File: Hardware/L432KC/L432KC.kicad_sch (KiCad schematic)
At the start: 41 parts, among them J1 L4_G4, J2 USB_B_Micro, J3 JTAG, J4 3v3, J5 GND, J6 Conn_01x09, J7 Conn_01x08, J8 TVCC, J9 LogicAna, U1 AD8531ARTZ, U2 SRV05-4, U3 NUCLEO-L432KC, U4 TXB0304RUT, U5 TXB0304RUT

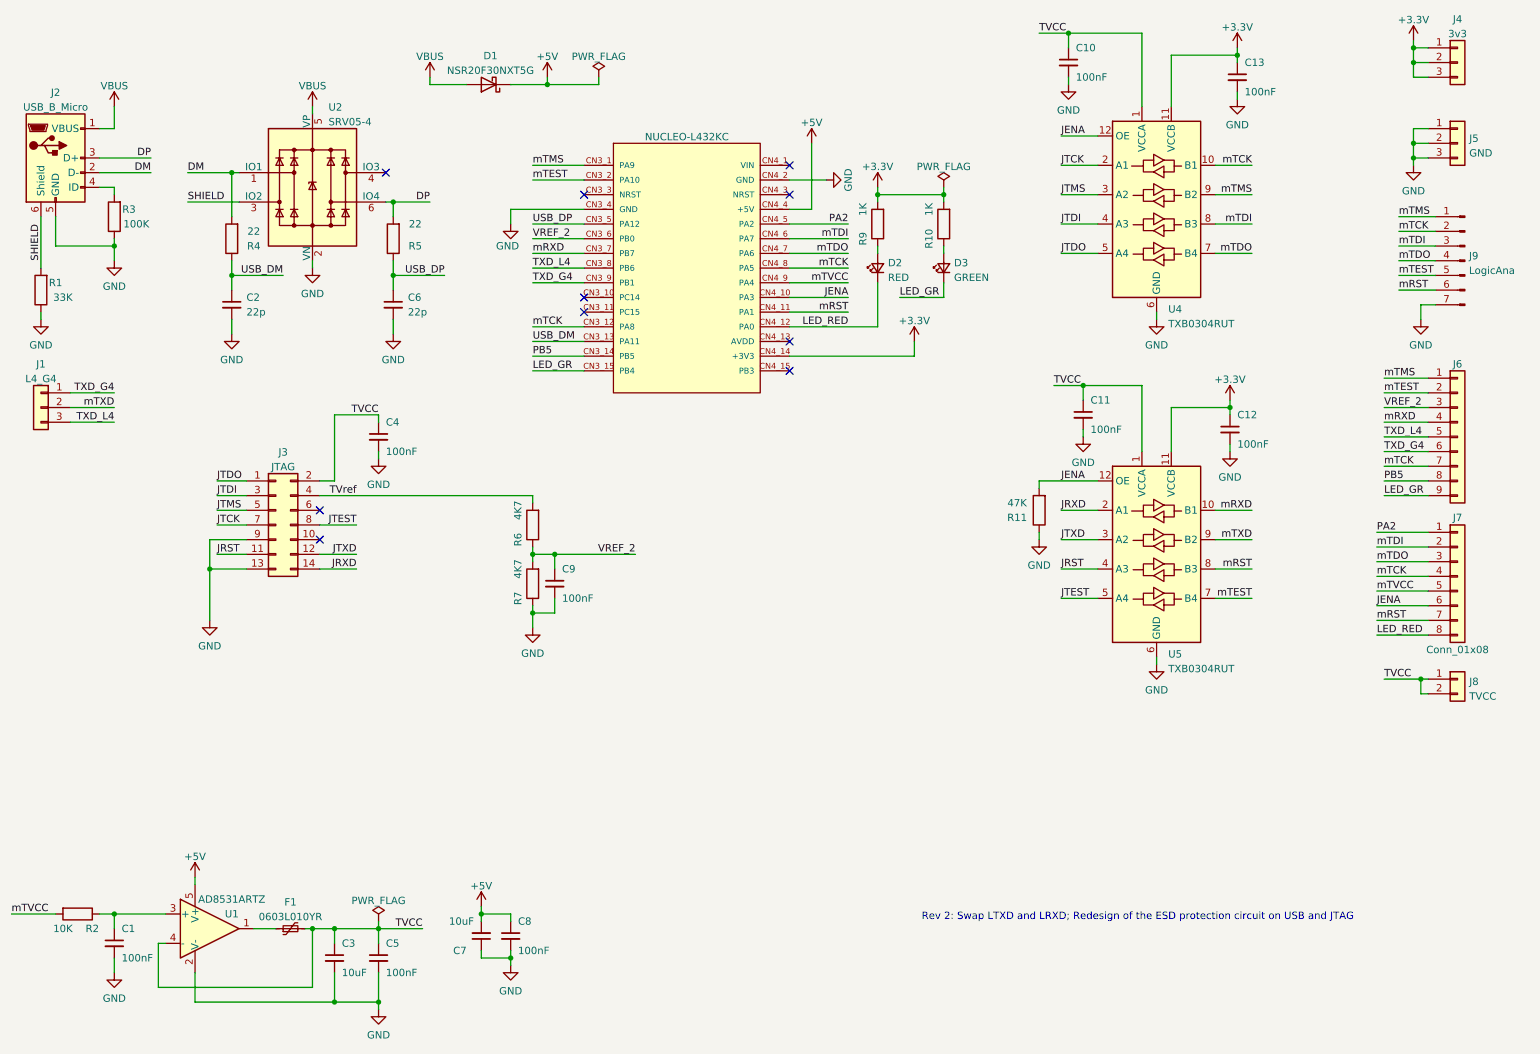
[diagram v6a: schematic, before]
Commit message: Updated L432KC/G431K6 prototype board.
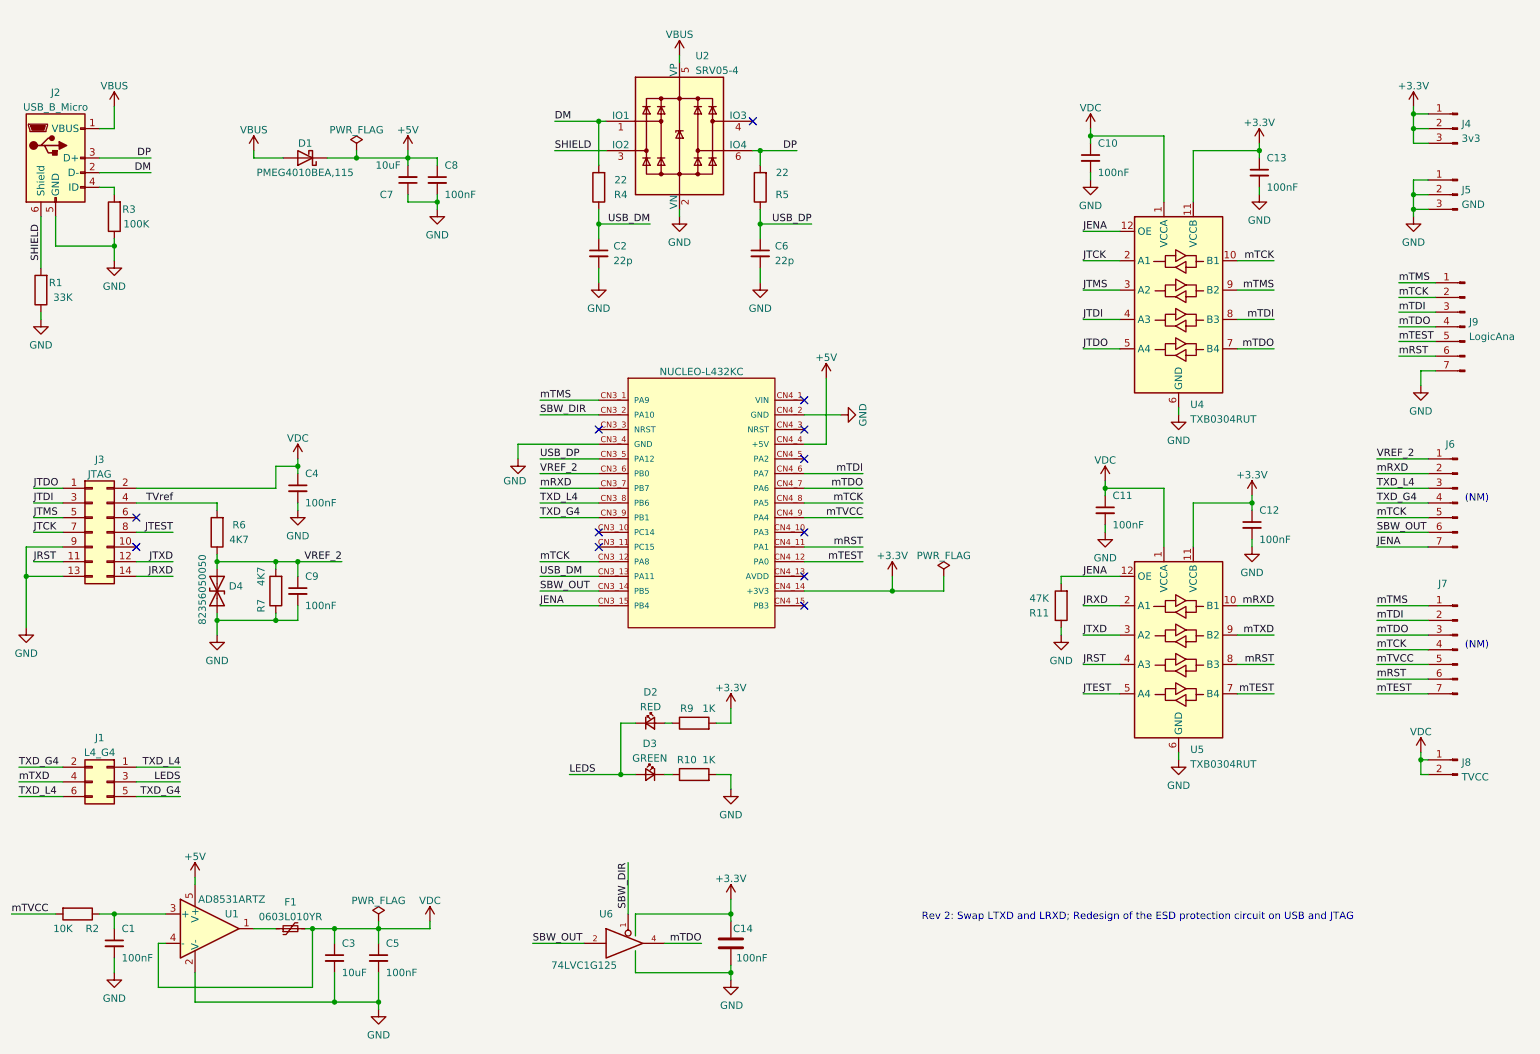
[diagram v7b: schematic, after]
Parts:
- added C14: 100nF, Capacitor_SMD:C_0603_1608Metric_Pad1.08x0.95mm_HandSolder, symbol Device:C
- added D4: 82356050050, Diode_SMD:D_0603_1608Metric_Pad1.05x0.95mm_HandSolder, symbol Device:D_TVS
- added U6: 74LVC1G125, Package_TO_SOT_SMD:SOT-23-5_HandSoldering, symbol 74xGxx:74LVC1G125
- D1: value NSR20F30NXT5G -> PMEG4010BEA,115; footprint Diode_SMD:D_0603_1608Metric_Pad1.05x0.95mm_HandSolder -> Diode_SMD:D_SOD-323
- J1: footprint Connector_PinHeader_2.54mm:PinHeader_1x03_P2.54mm_Vertical -> Connector_PinHeader_2.54mm:PinHeader_2x03_P2.54mm_Vertical; symbol Connector_Generic:Conn_01x03 -> Connector_Generic:Conn_02x03_Odd_Even
- J4, J5: symbol Connector_Generic:Conn_01x03 -> Connector:Conn_01x03_Male
- J6: value Conn_01x09 -> Conn_01x07; footprint Connector_PinHeader_2.54mm:PinHeader_1x09_P2.54mm_Vertical -> Connector_PinHeader_2.54mm:PinHeader_1x07_P2.54mm_Vertical; symbol Connector_Generic:Conn_01x09 -> Connector:Conn_01x07_Male
- J7: value Conn_01x08 -> Conn_01x07_Male; footprint Connector_PinHeader_2.54mm:PinHeader_1x08_P2.54mm_Vertical -> Connector_PinHeader_2.54mm:PinHeader_1x07_P2.54mm_Vertical; symbol Connector_Generic:Conn_01x08 -> Connector:Conn_01x07_Male
- J8: symbol Connector_Generic:Conn_01x02 -> Connector:Conn_01x02_Male
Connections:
- net +3.3V: now also C14.2, U6.5 (VCC); no longer R10.2
- net GND: now also R10.2, C14.1, D4.1 (A1), U6.3 (GND)
- net JENA: now also J6.7 (Pin_7), U3.CN3_15 (PB4); no longer J7.6 (Pin_6), U3.CN4_10 (PA3)
- net TXD_G4: now also J1.2 (Pin_2), J1.5 (Pin_5), J6.4 (Pin_4); no longer J1.1 (Pin_1), J6.6 (Pin_6)
- net TXD_L4: now also J1.1 (Pin_1), J1.6 (Pin_6), J6.3 (Pin_3); no longer J1.3 (Pin_3), J6.5 (Pin_5)
- net VREF_2: now also J6.1 (Pin_1), D4.2 (A2); no longer J6.3 (Pin_3)
- net mRST: now also J7.6 (Pin_6); no longer J7.7 (Pin_7)
- net mRXD: now also J6.2 (Pin_2); no longer J6.4 (Pin_4)
- net mTCK: now also J6.5 (Pin_5); no longer J6.7 (Pin_7)
- net mTDO: now also U6.4
- net mTEST: now also J7.7 (Pin_7), U3.CN4_12 (PA0); no longer J6.2 (Pin_2), U3.CN3_2 (PA10)
- net mTMS: now also J7.1 (Pin_1); no longer J6.1 (Pin_1)
- net mTXD: now also J1.4 (Pin_4); no longer J1.2 (Pin_2)
- net at R10.1: now also D3.1 (K); no longer D3.2 (A)
- removed net LED_GR: D3.1 (K), J6.9 (Pin_9), U3.CN3_15 (PB4)
- removed net LED_RED: D2.1 (K), J7.8 (Pin_8), U3.CN4_12 (PA0)
- net PA2: no longer names the net of U3.CN4_5 (PA2)
- net PA2: no longer J7.1 (Pin_1)
- net PB5 renamed SBW_OUT
- net SBW_OUT: now also J6.6 (Pin_6), U6.2; no longer J6.8 (Pin_8)
- net TVCC renamed VDC
- new net LEDS: D2.1 (K), D3.2 (A), J1.3 (Pin_3)
- new net SBW_DIR: U3.CN3_2 (PA10), U6.1
- no-connect marks 10 -> 12
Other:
- note added: "(NM)"
- moved on the sheet: C10, C11, C12, C13, C2, C4, C6, C7, C8, C9, D1, D2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

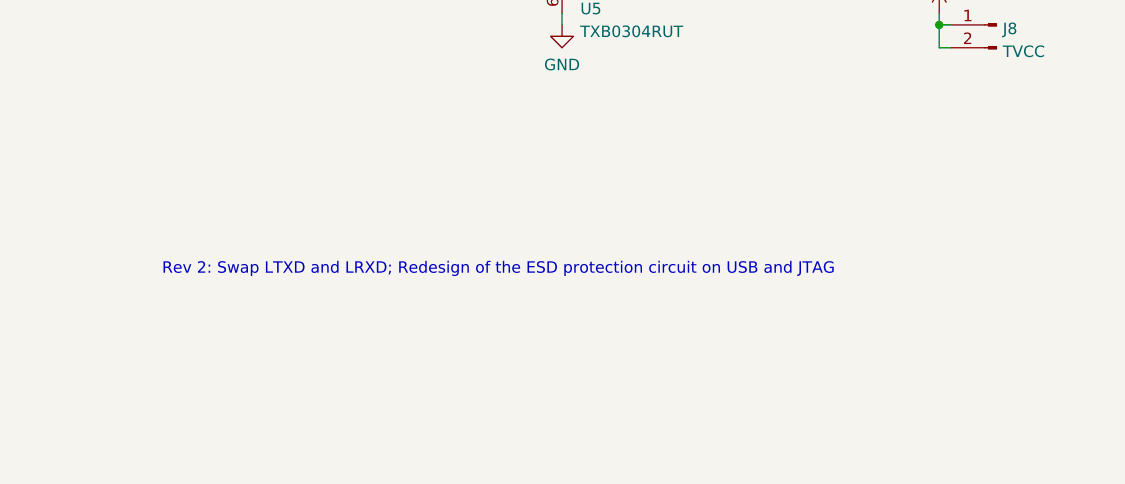
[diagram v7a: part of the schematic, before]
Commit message: Updated L432KC/G431K6 prototype board.
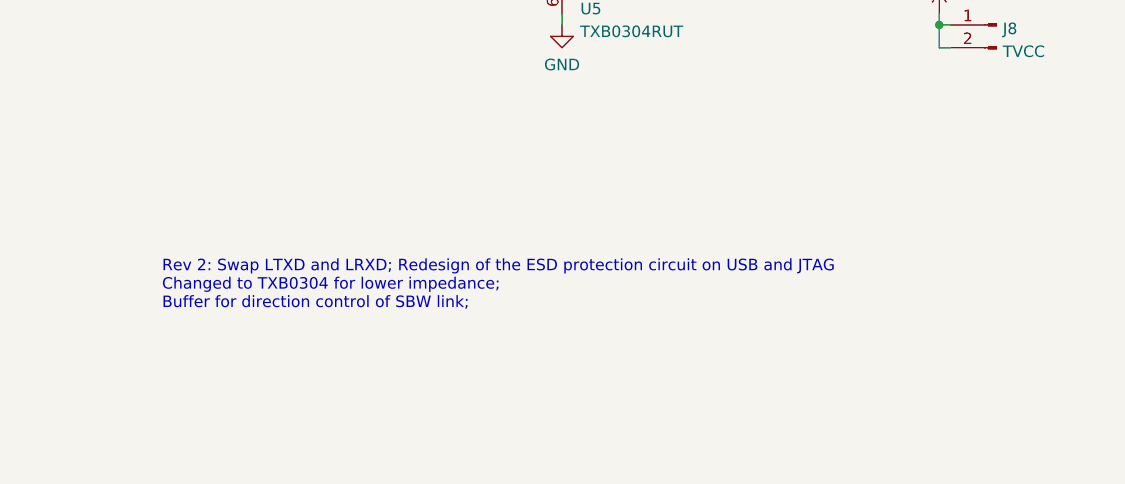
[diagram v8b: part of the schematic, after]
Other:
- note added: "Rev 2: Swap LTXD and LRXD; Redesign of the ESD protection circuit on USB and JTAG Changed to TXB0304 for lower impedance; Buffer for direction control of SBW link;"
- note removed: "Rev 2: Swap LTXD and LRXD; Redesign of the ESD protection circuit on USB and JTAG"
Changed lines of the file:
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@@
     (effects (font (size 1.27 1.27)) (justify left bottom))
   )
-  (text "Rev 2: Swap LTXD and LRXD; Redesign of the ESD protection circuit on USB and JTAG"
-    (at 179.07 170.18 0)
+  (text "Rev 2: Swap LTXD and LRXD; Redesign of the ESD protection circuit on USB and JTAG\nChanged to TXB0304 for lower impedance;\nBuffer for direction control of SBW link;"
+    (at 179.07 173.99 0)
     (effects (font (size 1.27 1.27)) (justify left bottom))
   )
@@
   (symbol (lib_id "power:VDC") (at 210.82 93.98 0) (unit 1)
     (in_bom yes) (on_board yes) (fields_autoplaced)
-    (property "Reference" "#PWR?" (id 0) (at 210.82 96.52 0)
+    (property "Reference" "#PWR0106" (id 0) (at 210.82 96.52 0)
       (effects (font (size 1.27 1.27)) hide)
     )
@@
   (symbol (lib_id "power:VDC") (at 265.43 140.97 0) (unit 1)
     (in_bom yes) (on_board yes) (fields_autoplaced)
-    (property "Reference" "#PWR?" (id 0) (at 265.43 143.51 0)
+    (property "Reference" "#PWR0102" (id 0) (at 265.43 143.51 0)
       (effects (font (size 1.27 1.27)) hide)
     )
@@
       (reference "#PWR0101") (unit 1) (value "VDC") (footprint "")
     )
+    (path "/86b06f5c-2a31-4b5f-81f5-e1b28d250a5f"
+      (reference "#PWR0102") (unit 1) (value "VDC") (footprint "")
+    )
     (path "/d26c7eea-a8ed-4810-8eda-c874f2952743"
       (reference "#PWR0103") (unit 1) (value "+3.3V") (footprint "")
@@
     )
     (path "/5aee9e56-1369-4dfa-b321-603177fc9903"
-      (reference "#PWR?") (unit 1) (value "VDC") (footprint "")
-    )
-    (path "/86b06f5c-2a31-4b5f-81f5-e1b28d250a5f"
-      (reference "#PWR?") (unit 1) (value "VDC") (footprint "")
+      (reference "#PWR0106") (unit 1) (value "VDC") (footprint "")
     )
     (path "/5911ba98-0620-49a4-af6c-7be24e24119e"
